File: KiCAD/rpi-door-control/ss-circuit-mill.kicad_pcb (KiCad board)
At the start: 2 copper layers, 26 parts, among them IC1 4N35, J1 RJ45, P1 CONN_13X2, P2 CONN_2, P3 CONN_2, P4 CONN_2, Q1 2N3904, Q2 2N3904, SW1 SW_PUSH, U1 RELAY

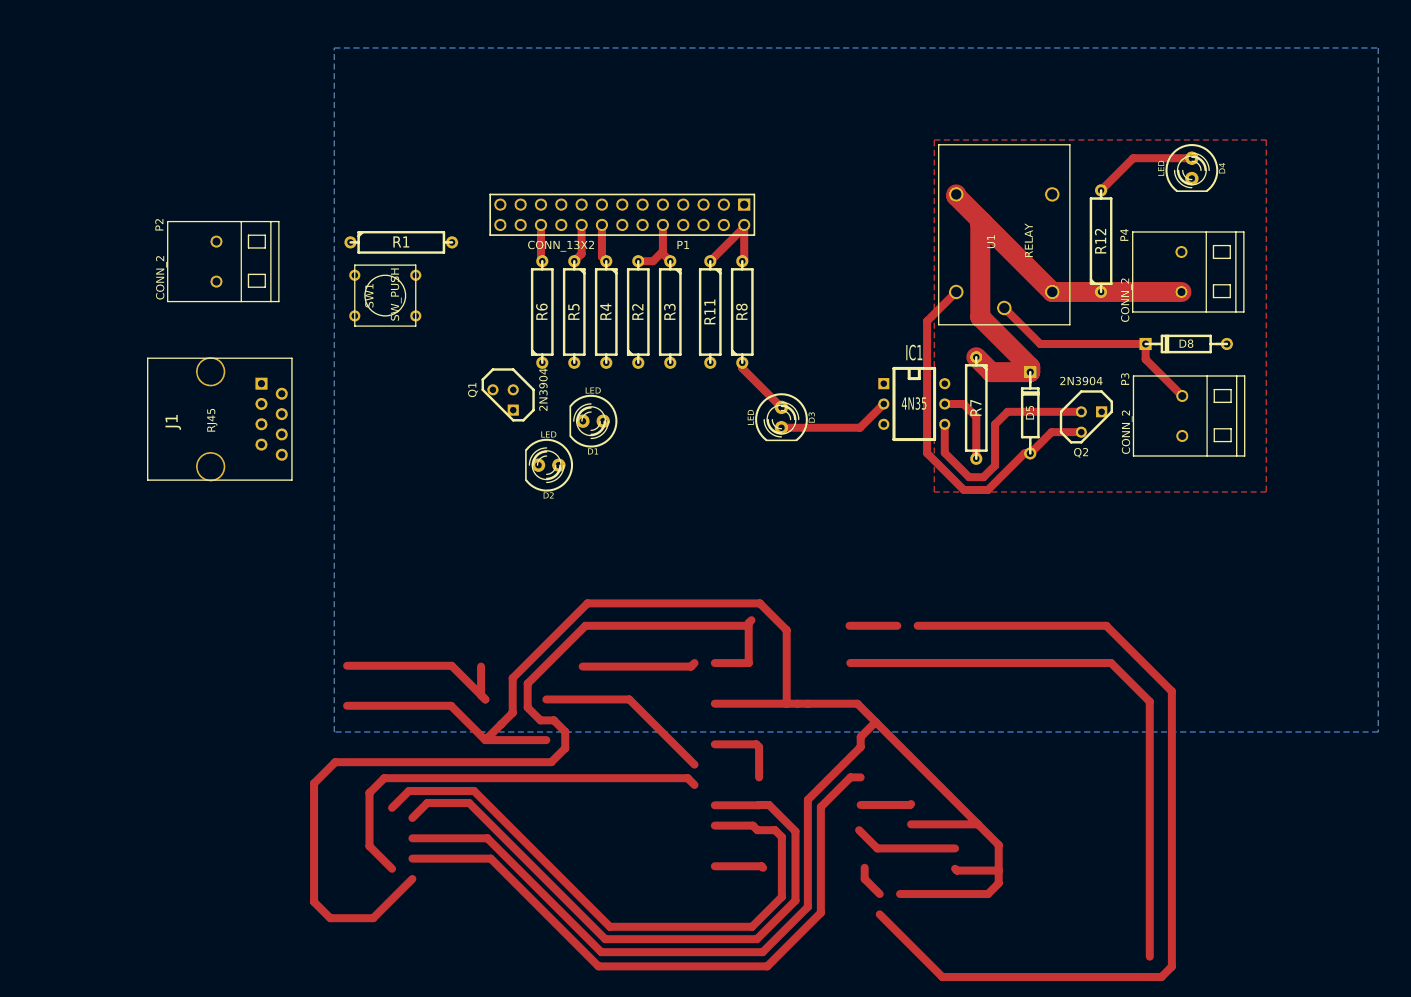
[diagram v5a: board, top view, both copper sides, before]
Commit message: Still need to connect ground and 5v
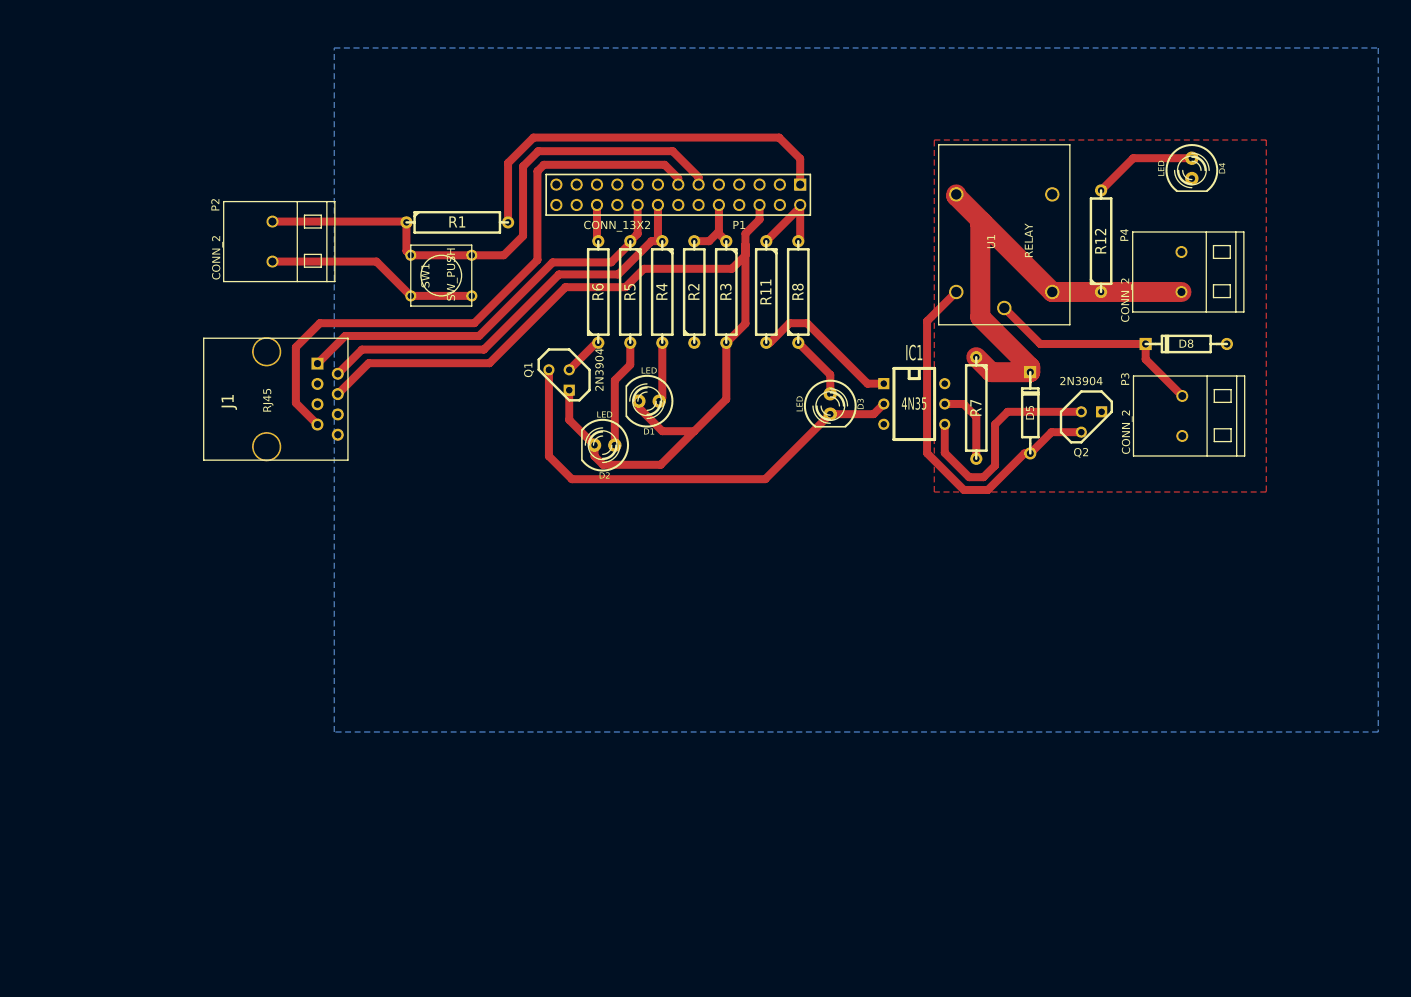
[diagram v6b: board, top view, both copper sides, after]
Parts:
- moved P2 7.43 mm to (64.8, 78.7)
- moved D1 7.43 mm to (111.8, 98.7)
- moved D2 7.43 mm to (106.3, 104.2)
- moved J1 7.43 mm to (64.0, 98.4)
- moved P1 7.43 mm to (115.5, 72.8)
- moved Q1 7.43 mm to (100.6, 96.0)
- moved R1 7.43 mm to (87.9, 76.3)
- moved R11 7.43 mm to (126.5, 85.0)
- moved R2 7.43 mm to (117.5, 85.0)
- moved R3 7.43 mm to (121.5, 85.0)
- moved R4 7.43 mm to (113.5, 85.0)
- moved R5 7.43 mm to (109.5, 85.0)
- moved R6 7.43 mm to (105.5, 85.0)
- moved R8 7.43 mm to (130.5, 85.0)
- moved SW1 7.43 mm to (85.9, 83.0)
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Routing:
- net (no net): track 927.3 -> 0.00 mm
- net GND: track 0.00 -> 151.0 mm
- net /BELL: track 0.00 -> 76.0 mm
- net /GPIO17: track 0.00 -> 69.9 mm
- net +3.3V: track 0.00 -> 49.6 mm
- net /GPIO23: track 4.75 -> 52.2 mm
- net /GPIO24: track 4.91 -> 50.5 mm
- net N-0000025: track 14.0 -> 57.7 mm
- net N-0000019: track 0.00 -> 18.8 mm
- net N-000001: track 0.00 -> 13.6 mm
- net N-000002: track 0.00 -> 7.46 mm
- net N-000003: track 0.00 -> 5.03 mm

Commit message: Very close to the final layout.  Just have to reposition LEDs, put some labels, and make some 3D models.
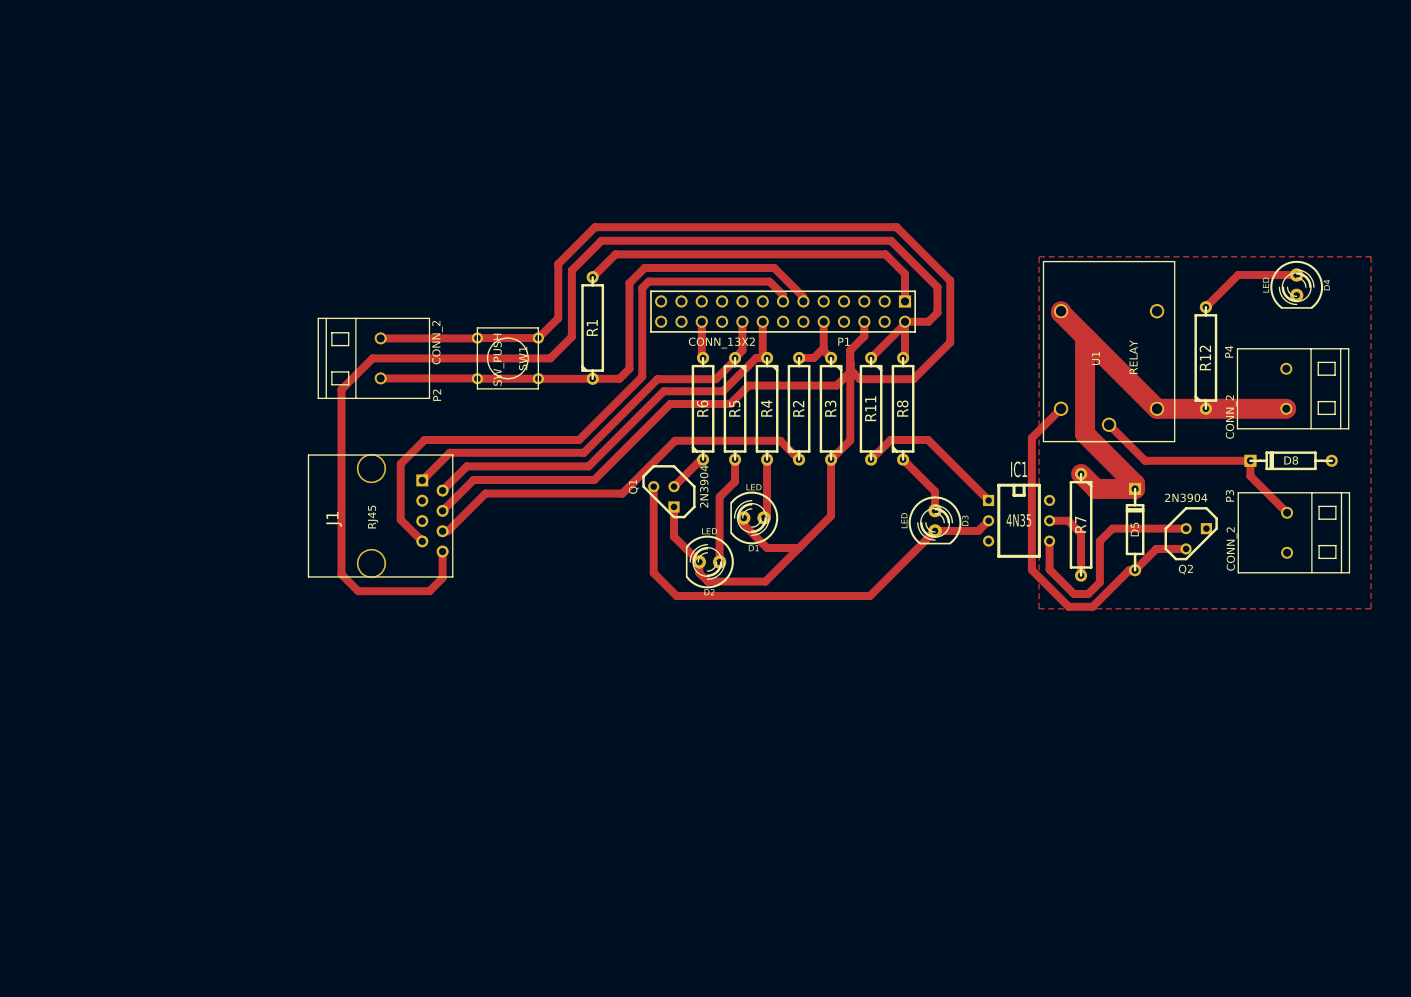
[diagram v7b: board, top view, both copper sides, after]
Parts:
- moved R1 21.5 mm to (104.8, 89.5), turned to 90 degrees
- moved P2 19.9 mm to (78.3, 93.3), turned to 90 degrees
- moved D4 19.6 mm to (192.8, 84.2)
- moved D5 19.6 mm to (172.6, 114.7)
- moved P1 19.6 mm to (128.6, 87.5)
- moved D1 19.6 mm to (125.0, 113.2)
- moved D2 19.6 mm to (119.4, 118.8)
- moved J1 19.6 mm to (77.2, 113.0)
- moved Q1 19.6 mm to (113.7, 110.6)
- moved D3 19.6 mm to (147.6, 113.6)
- moved D8 19.6 mm to (192.1, 106.1)
- moved IC1 19.6 mm to (158.1, 113.6)
- moved P3 19.6 mm to (191.6, 115.1)
- moved P4 19.6 mm to (191.5, 97.1)
- moved Q2 19.6 mm to (180.2, 115.8)
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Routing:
- net +5V: track 10.9 -> 148.7 mm
- net GND: track 151.0 -> 231.4 mm
- net /RFID TXD: track 0.00 -> 50.2 mm
- net +3.3V: track 49.6 -> 44.7 mm
- net /GPIO17: track 69.9 -> 66.9 mm
- removed copper zone on B.Cu, net (none)

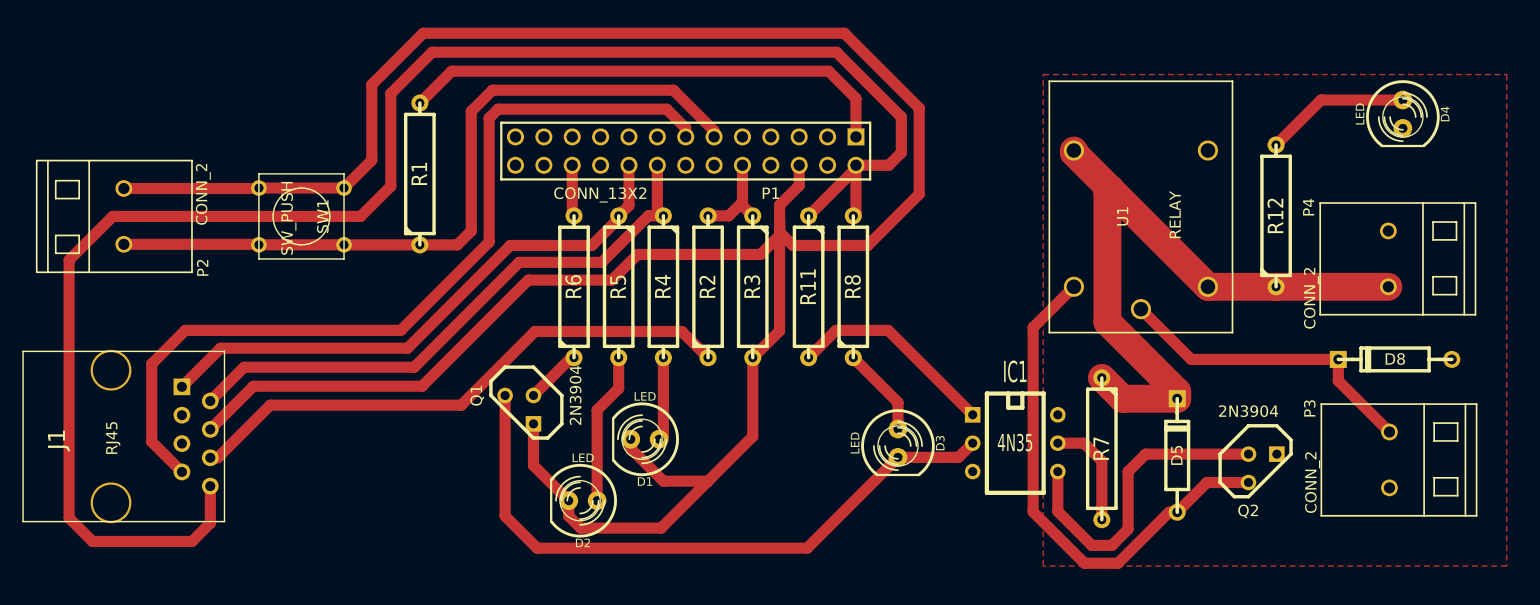
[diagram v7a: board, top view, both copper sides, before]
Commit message: Clean up single sided pcb, change version numbers
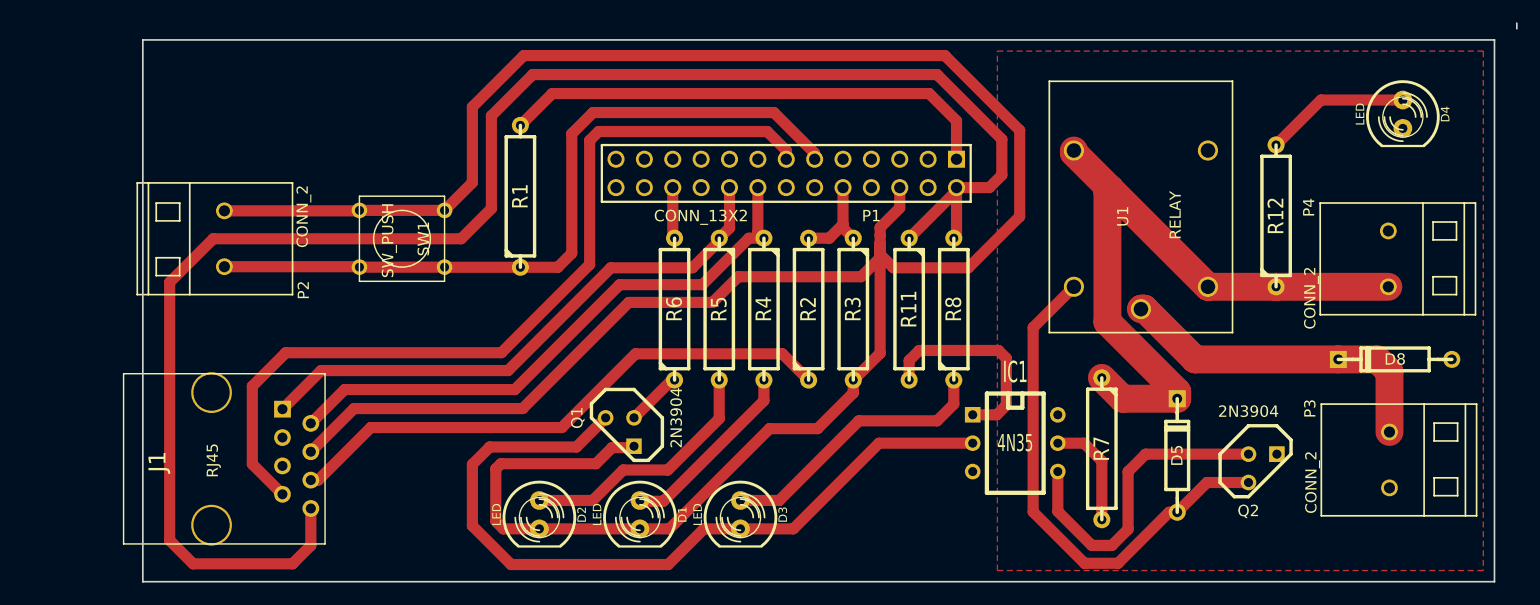
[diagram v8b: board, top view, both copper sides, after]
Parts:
- moved D3 15.5 mm to (133.5, 120.0)
- moved J1 9.22 mm to (86.2, 115.0)
- moved P1 9.22 mm to (137.6, 89.5)
- moved P2 9.22 mm to (87.3, 95.3)
- moved Q1 9.22 mm to (122.7, 112.6)
- moved R1 9.22 mm to (113.8, 91.5)
- moved R11 9.22 mm to (148.6, 101.6)
- moved R2 9.22 mm to (139.6, 101.6)
- moved R3 9.22 mm to (143.6, 101.6)
- moved R4 9.22 mm to (135.6, 101.6)
- moved R5 9.22 mm to (131.6, 101.6)
- moved R6 9.22 mm to (127.6, 101.6)
- moved R8 9.22 mm to (152.6, 101.6)
- moved SW1 9.22 mm to (103.2, 95.3)
- moved D1 6.76 mm to (124.5, 120.0), turned to 270 degrees
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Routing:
- net N-0000026: track 8.04 -> 24.8 mm
- net N-0000025: track 57.7 -> 69.9 mm
- net GND: track 231.4 -> 241.9 mm
- net N-000002: track 7.46 -> 16.7 mm
- net N-000001: track 13.6 -> 22.6 mm
- net N-0000027: track 27.9 -> 30.0 mm
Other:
- board outline added: 123 x 50 mm
